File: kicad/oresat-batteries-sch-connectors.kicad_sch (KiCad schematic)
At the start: 13 parts, among them J1 J-SAMTEC-TFM-120-X1-XXX-D-RA, SW1 OMRON-D2F-L3-D-LEFT, SW2 OMRON-D2F-L3-D-RIGHT, SW3 OMRON-D2F-L3-D-LEFT, SW4 OMRON-D2F-L3-D-RIGHT

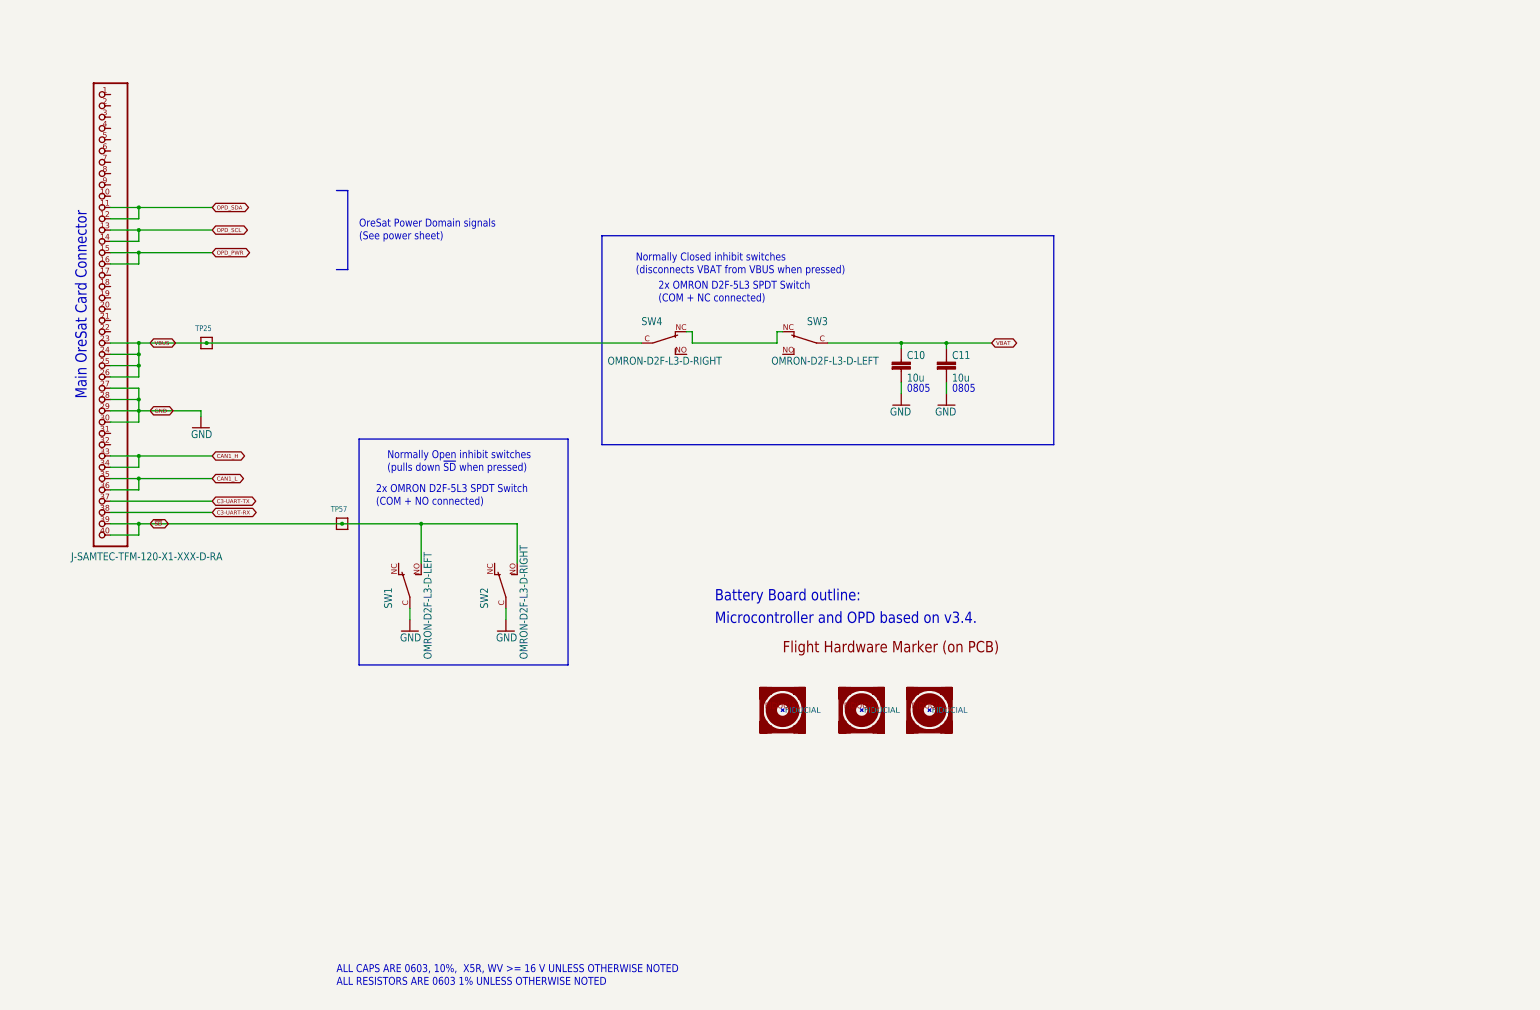
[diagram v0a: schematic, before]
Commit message: Kicad import try #3. Now with DXFs from custom EAGLE layers. Schematic worksheets and names updated.
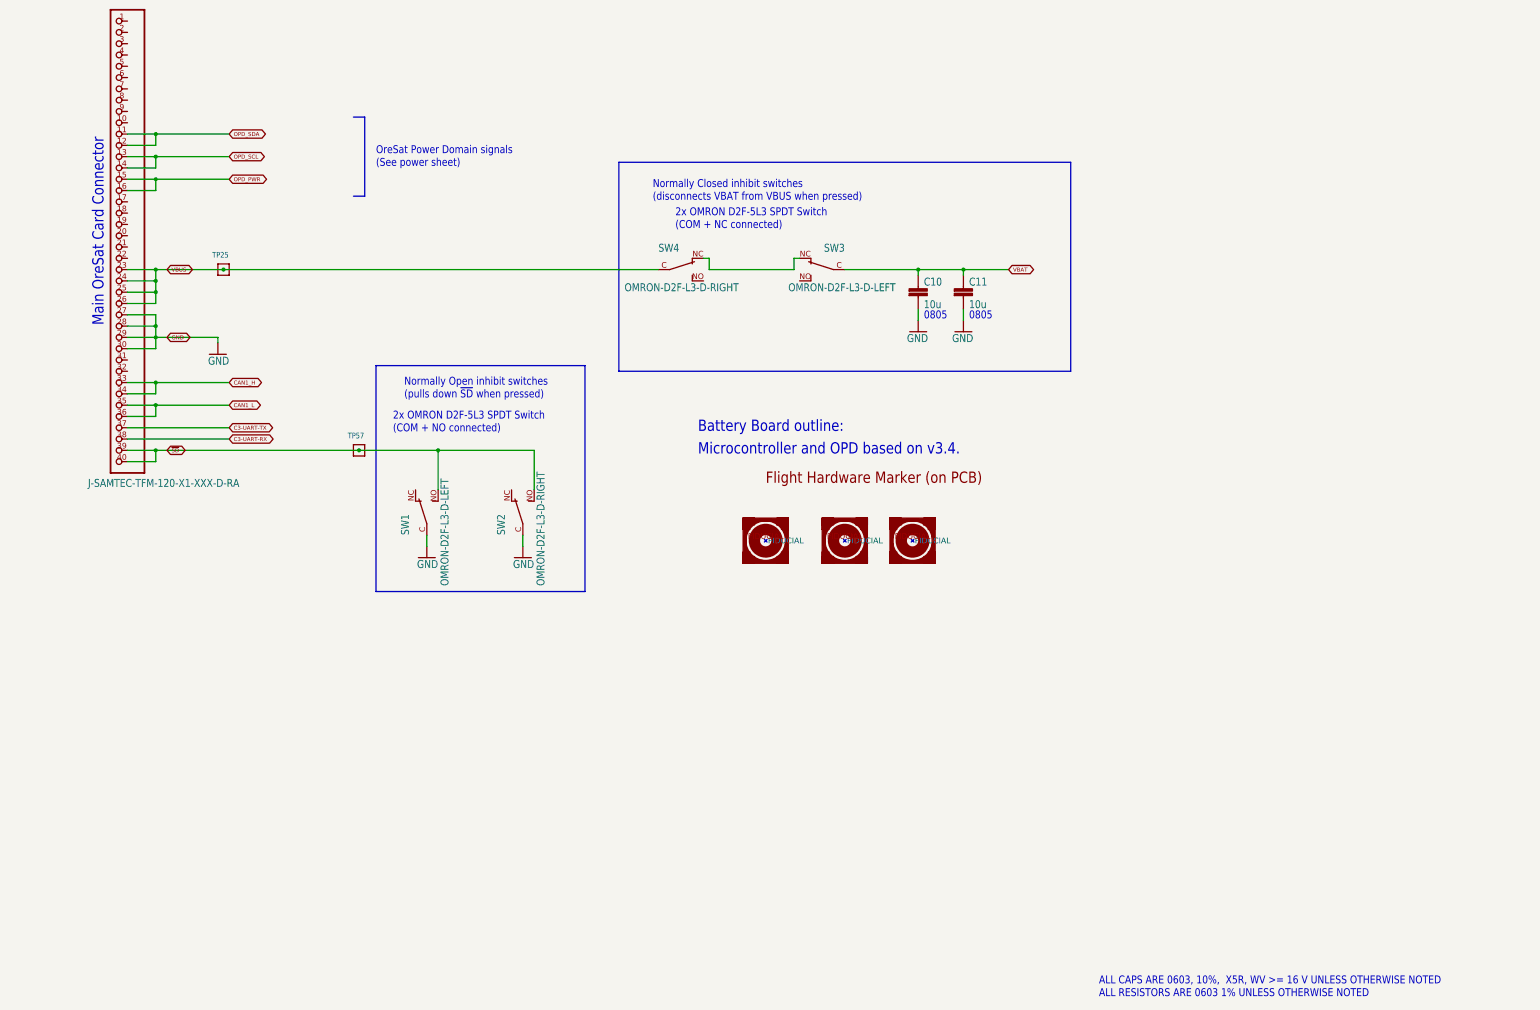
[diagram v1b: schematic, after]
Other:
- title: OreSat Battery Card - Connectors -> OreSat Battery Card

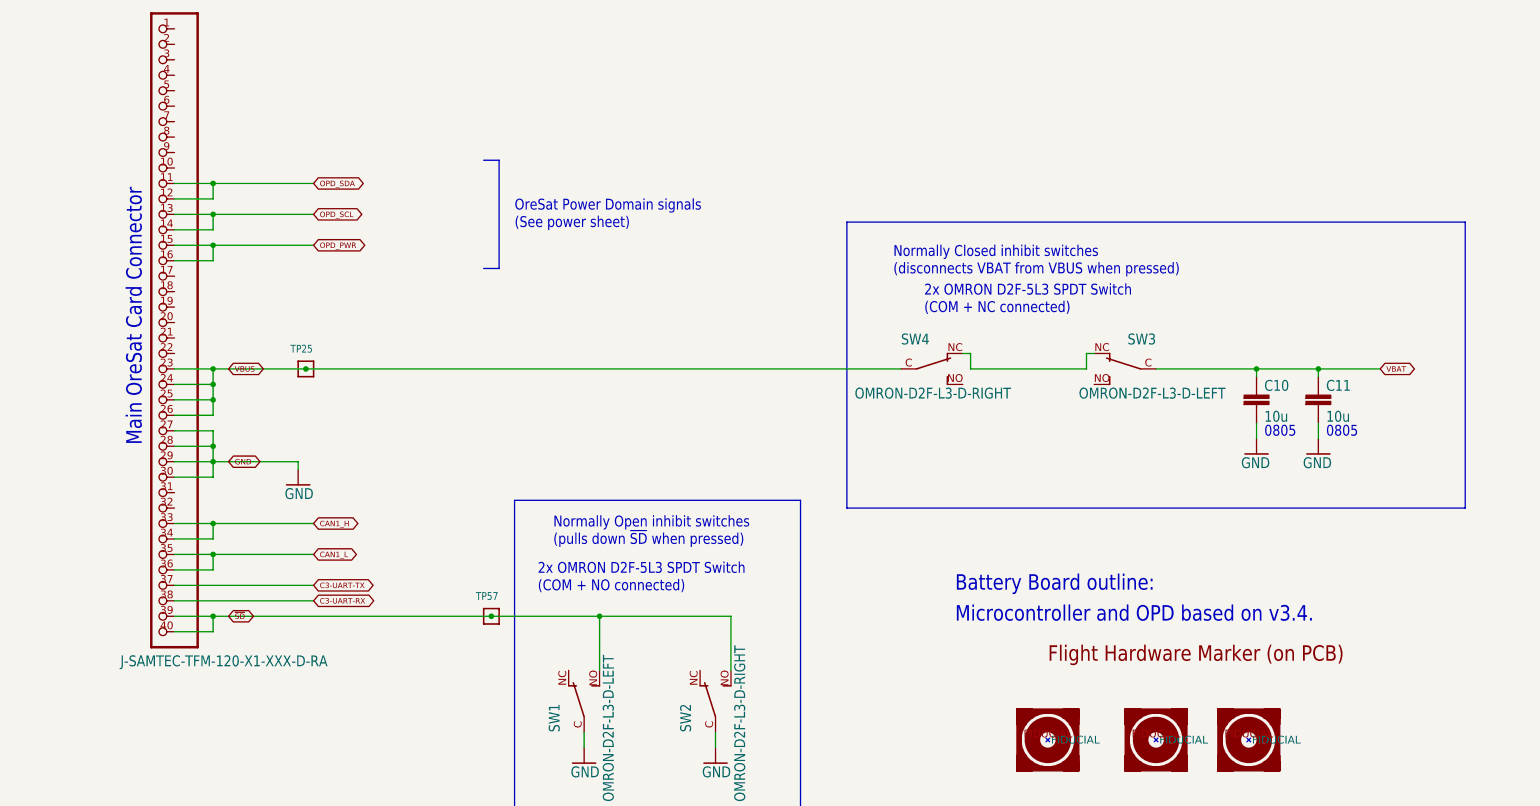
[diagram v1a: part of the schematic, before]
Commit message: Move main connector to kicad libraries; start updating text size.
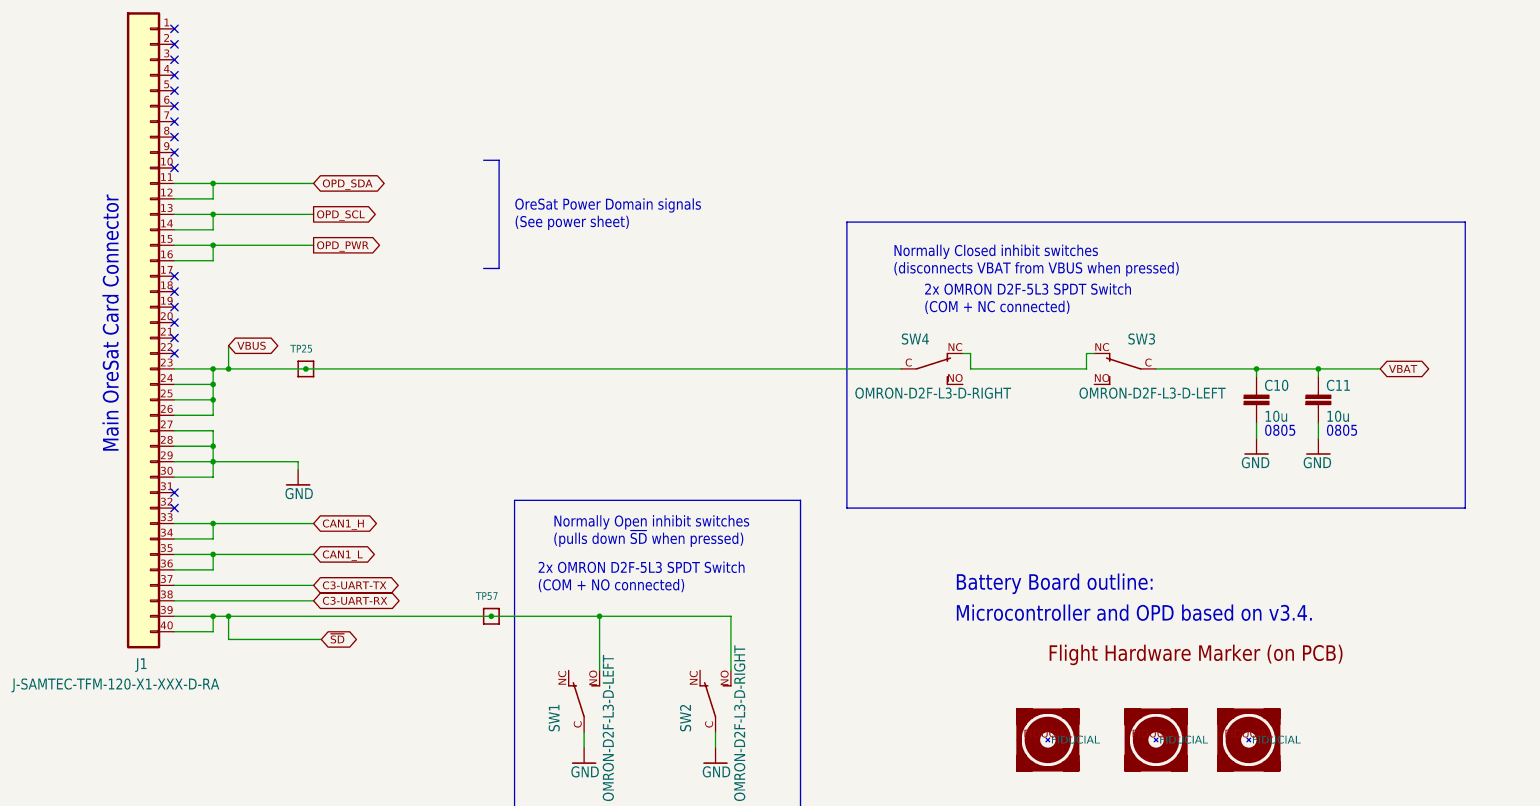
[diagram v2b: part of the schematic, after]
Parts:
- J1: footprint oresat-batteries:J-SAMTEC-TFM-120-X1-XXX-D-RA -> oresat-connectors:J-SAMTEC-TFM-120-X1-XXX-D-RA; symbol oresat-batteries-eagle-import:J-SAMTEC-TFM-120-X1-XXX-D-RA -> oresat-connectors:J-SAMTEC-TFM-120-01-L-D-RA
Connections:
- no-connect marks 0 -> 18
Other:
- title: OreSat Battery Card -> OreSat Battery Card - Connectors

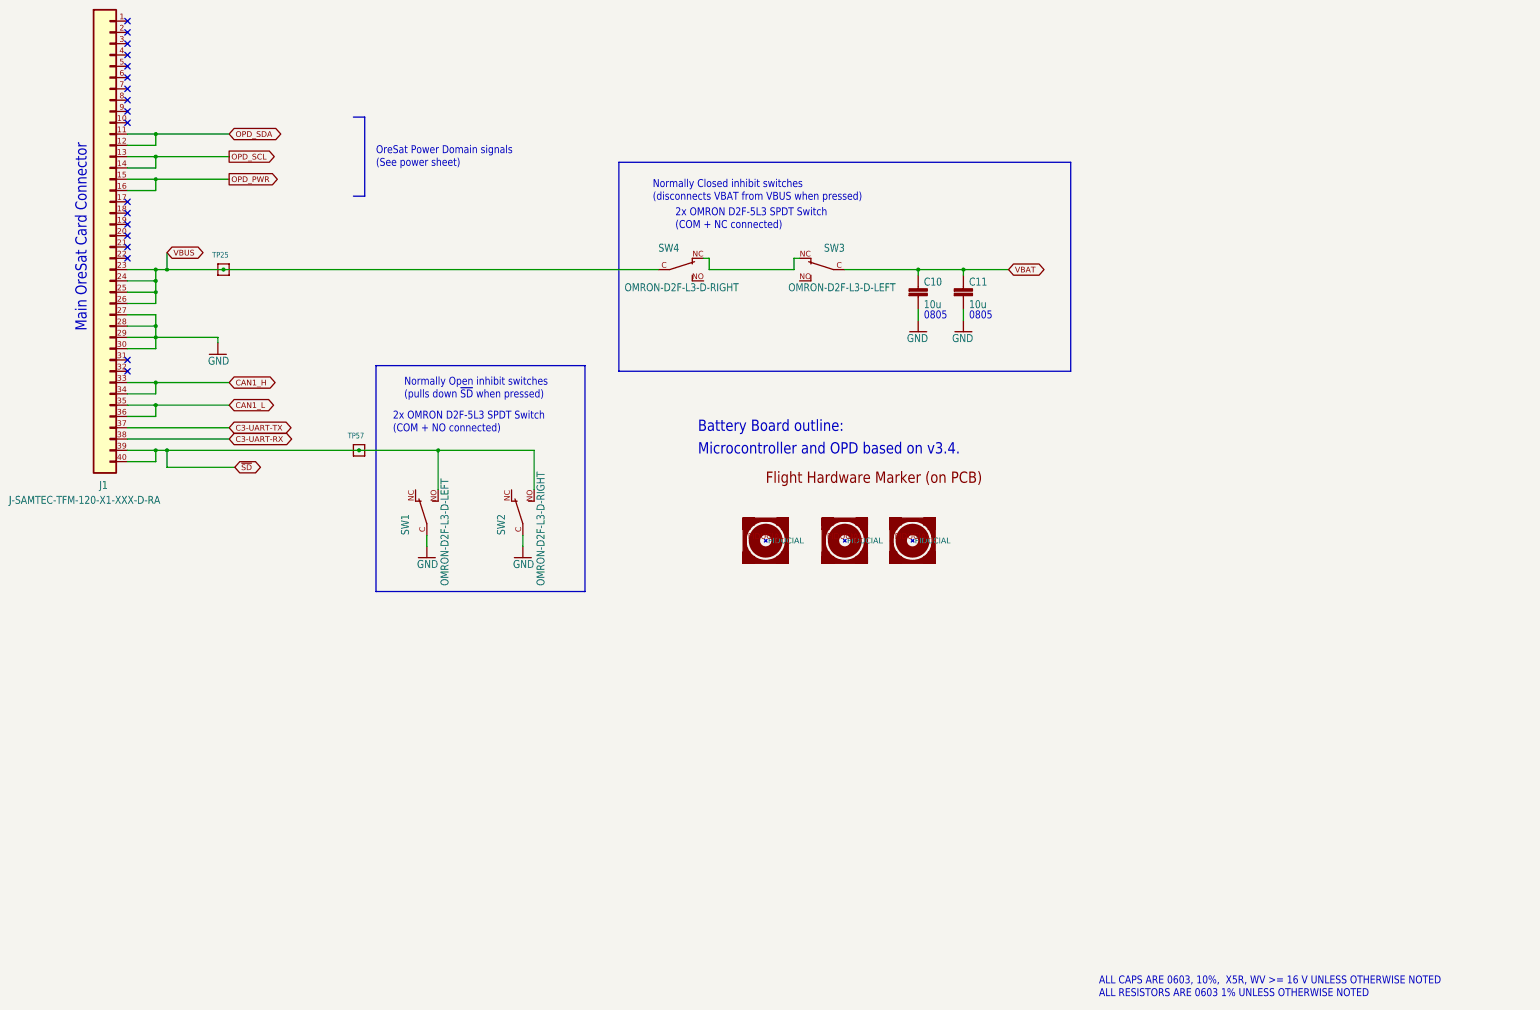
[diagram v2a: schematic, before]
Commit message: Transferred connector page to oresat-kicad. Added correct card outline.
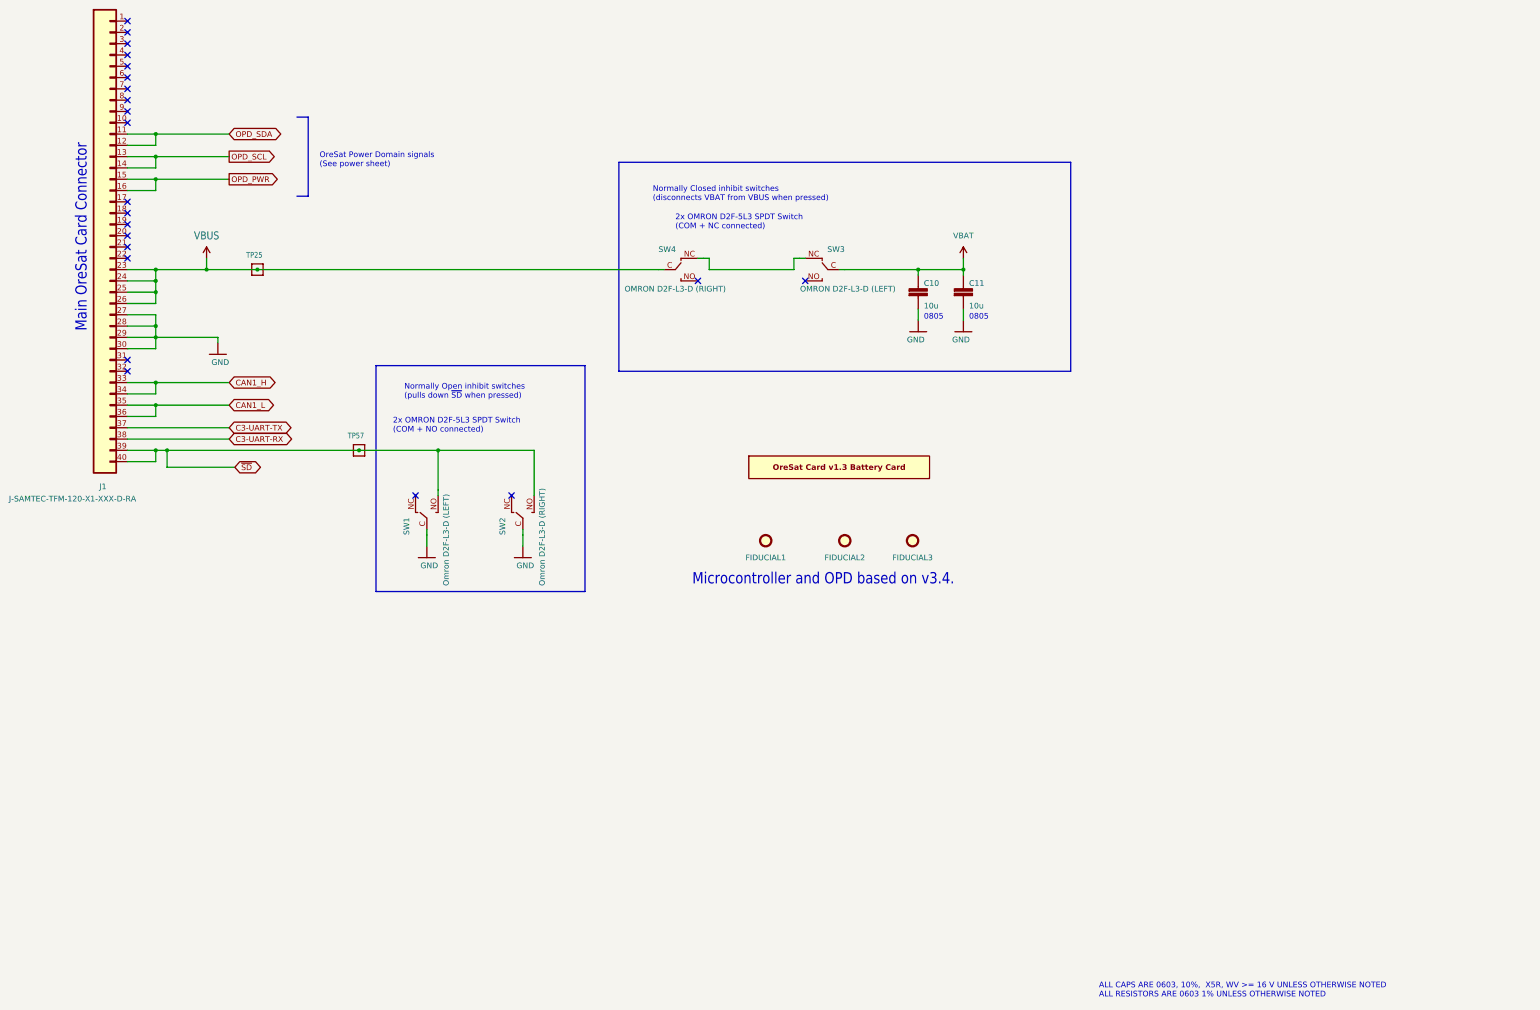
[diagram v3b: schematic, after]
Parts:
- removed U$1: FLIGHMARKERNEW, oresat-batteries:FLIGHTMARKER_NEW_BOARDS, symbol oresat-batteries-eagle-import:FLIGHMARKERNEW
- added PCB1: ORESAT-CARD-V1.3-BATTERY, oresat-pcbs:ORESAT-CARD-V1.3-BATTERY-V3.0, symbol oresat-pcbs:ORESAT-CARD-V1.3-BATTERY
- FIDUCIAL1, FIDUCIAL2, FIDUCIAL3: footprint oresat-batteries:FIDUCIAL-1.0X2.0 -> Fiducial:Fiducial_1mm_Mask2mm; symbol oresat-batteries-eagle-import:FIDUCIAL-1.0X2.0 -> Mechanical:Fiducial
- SW1: value OMRON-D2F-L3-D-LEFT -> Omron D2F-L3-D (LEFT); footprint oresat-batteries:D2F-L3-D-HORIZONTAL-L -> oresat-misc:D2F-L3-D-HORIZONTAL-L; symbol oresat-batteries-eagle-import:OMRON-D2F-L3-D-LEFT -> oresat-misc:OMRON-D2F-L3-D-LEFT
- SW2: value OMRON-D2F-L3-D-RIGHT -> Omron D2F-L3-D (RIGHT); footprint oresat-batteries:D2F-L3-D-HORIZONTAL-R -> oresat-misc:D2F-L3-D-HORIZONTAL-R; symbol oresat-batteries-eagle-import:OMRON-D2F-L3-D-RIGHT -> oresat-misc:OMRON-D2F-L3-D-RIGHT
- SW3: value OMRON-D2F-L3-D-LEFT -> OMRON D2F-L3-D (LEFT); footprint oresat-batteries:D2F-L3-D-HORIZONTAL-L -> oresat-misc:D2F-L3-D-HORIZONTAL-L; symbol oresat-batteries-eagle-import:OMRON-D2F-L3-D-LEFT -> oresat-misc:OMRON-D2F-L3-D-LEFT
- SW4: value OMRON-D2F-L3-D-RIGHT -> OMRON D2F-L3-D (RIGHT); footprint oresat-batteries:D2F-L3-D-HORIZONTAL-R -> oresat-misc:D2F-L3-D-HORIZONTAL-R; symbol oresat-batteries-eagle-import:OMRON-D2F-L3-D-RIGHT -> oresat-misc:OMRON-D2F-L3-D-RIGHT
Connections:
- no-connect marks 18 -> 22
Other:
- note removed: "Battery Board outline:"
- moved on the sheet: TP25
